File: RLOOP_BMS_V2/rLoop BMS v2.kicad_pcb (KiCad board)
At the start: 2 copper layers, 77.5 x 133 mm, 273 parts, among them IC1 FXO-HC736R-1.000, IC2 SN74AUP1G74DCUR, IC3 ATA6870N-PLQW-1, IC4 ATA6870N-PLQW-1, IC5 ATA6870N-PLQW-1, J1 CONN_02X07, J2 2-640387-0, Q1 FDN337N, Q10 PMV20ENR, Q11 PMV20ENR, Q12 PMV20ENR, Q13 PMV20ENR, Q14 PMV20ENR, Q15 PMV20ENR, Q16 PMV20ENR, Q17 PMV20ENR, Q18 PMV20ENR, Q19 PMV20ENR, Q2 PMV20ENR, Q3 PMV20ENR, Q4 PMV20ENR, Q5 PMV20ENR, Q6 PMV20ENR, Q7 PMV20ENR, Q8 PMV20ENR, Q9 PMV20ENR, U1 VOS618A-2X001T

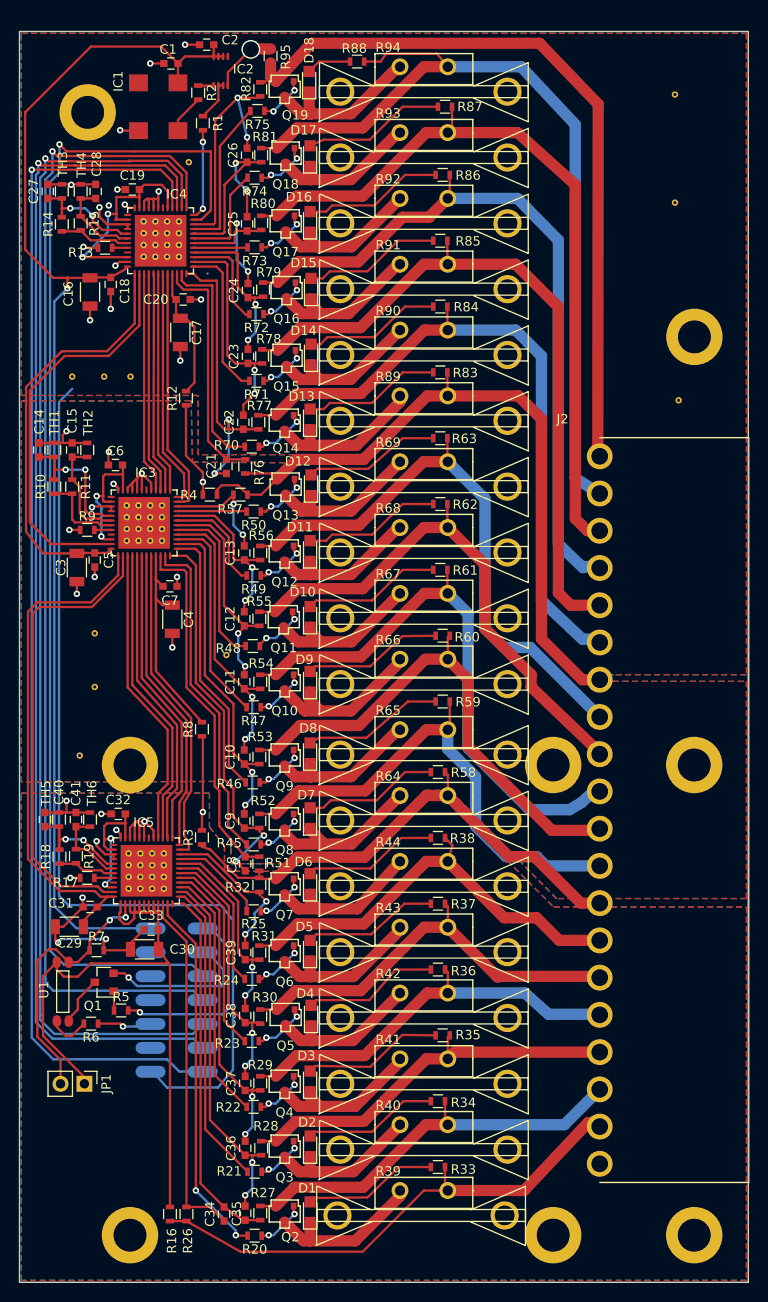
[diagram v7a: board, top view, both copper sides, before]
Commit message: More PCB Work
Should be done, needs final check on the stencil and solder mask around
the ata6870 thermal pad
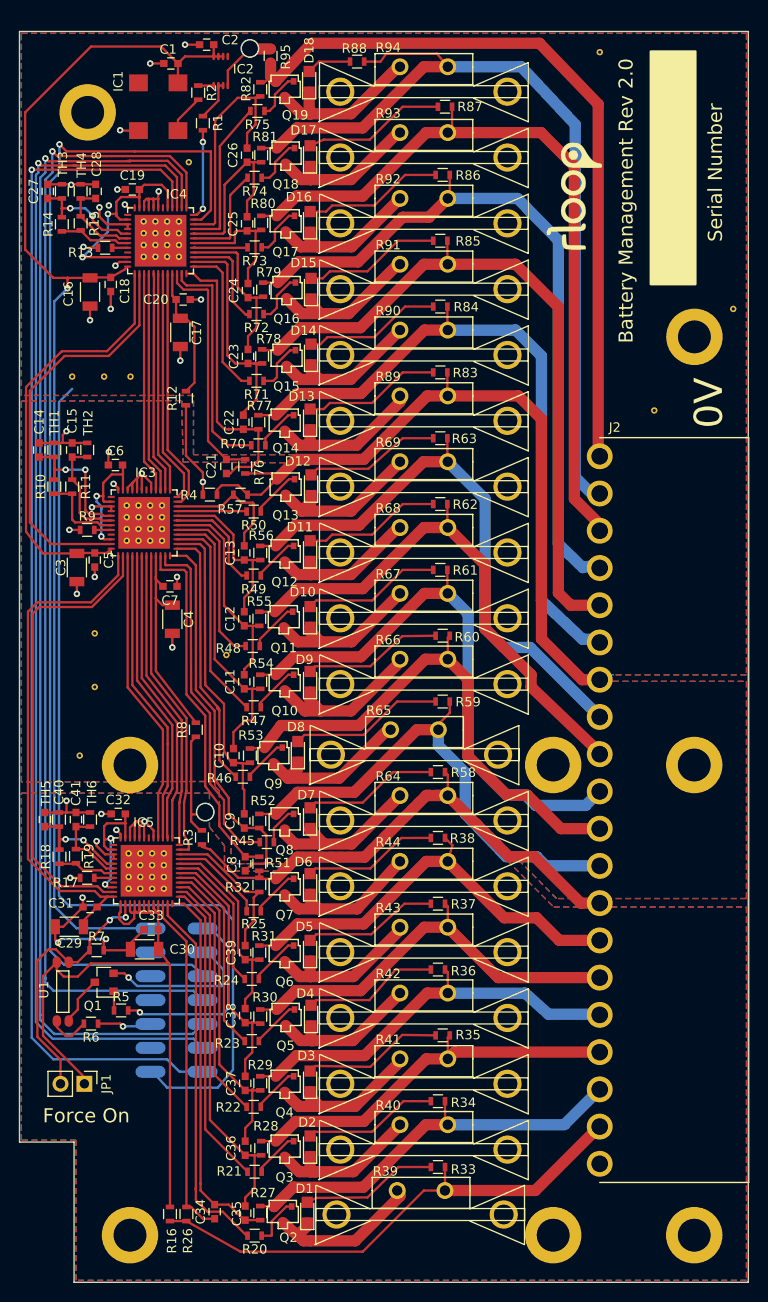
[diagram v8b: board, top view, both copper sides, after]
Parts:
- added G***: LOGO, rLoop_Footprints:rLoop_Logo, F.Cu at (109.0, 60.5)
- moved REF** 12.9 mm to (125.9, 72.5)
- moved REF** 9.18 mm to (111.7, 45.2)
- moved REF** 2.81 mm to (117.5, 83.3)
- moved R45 1.42 mm to (76.3, 129.2)
- moved D8 1.31 mm to (79.6, 119.6)
- moved Q9 1.23 mm to (77.0, 120.0)
- moved R46 1.21 mm to (73.8, 122.2)
- moved C10 1.16 mm to (72.8, 120.0)
- moved C34 1.03 mm to (70.8, 168.5)
- moved R53 1.01 mm to (74.5, 120.0)
- moved R65 1.00 mm to (92.0, 117.2)
- moved REF** 1.00 mm to (92.0, 119.9)
- moved R70 0.72 mm to (75.4, 87.0)
- moved R8 0.65 mm to (68.8, 117.2)
- moved D1 0.30 mm to (80.6, 168.6)
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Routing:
- net GND_3: track 51.7 -> 53.7 mm
- net /DISCHARGE Top/CELL_10: track 54.6 -> 56.4 mm
- net /CONTROLLER 1/MBAT3: track 16.1 -> 14.4 mm, vias 2 -> 0
- net /CONTROLLER 2/MBAT1: track 12.4 -> 14.0 mm, vias 2 -> 0
- net Net-(D8-Pad2): track 14.9 -> 16.4 mm
- net /CONTROLLER 1/MBAT6: track 32.1 -> 30.7 mm, vias 2 -> 0
- net /CONTROLLER 1/MBAT2: track 20.9 -> 19.5 mm, vias 2 -> 0
- net /DISCHARGE Top/DISCHARGE_2_6: track 35.6 -> 36.9 mm
- net Net-(Q8-Pad1): track 5.46 -> 4.20 mm, vias 2 -> 0
- net Net-(Q14-Pad1): track 5.99 -> 4.77 mm, vias 2 -> 0
- net /CONTROLLER 3/MBAT7: track 37.9 -> 36.8 mm
- net /DISCHARGE Top/CELL_18: track 55.5 -> 54.7 mm
- net /DISCHARGE Top/DISCHARGE_2_5: track 29.0 -> 28.2 mm
- net Net-(Q12-Pad1): track 5.77 -> 4.95 mm, vias 2 -> 0
- net Net-(Q9-Pad1): track 5.67 -> 4.87 mm, vias 2 -> 0
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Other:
- outline, holes or cut-outs redrawn
- board text added: "0V"
- board text added: "Battery Management Rev 2.0"
- board text added: "Force On"
- board text added: "Serial Number"
